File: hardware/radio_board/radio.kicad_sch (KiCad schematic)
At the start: 29 parts, among them J2 RF, J3 Shield, U1 MAX2769B

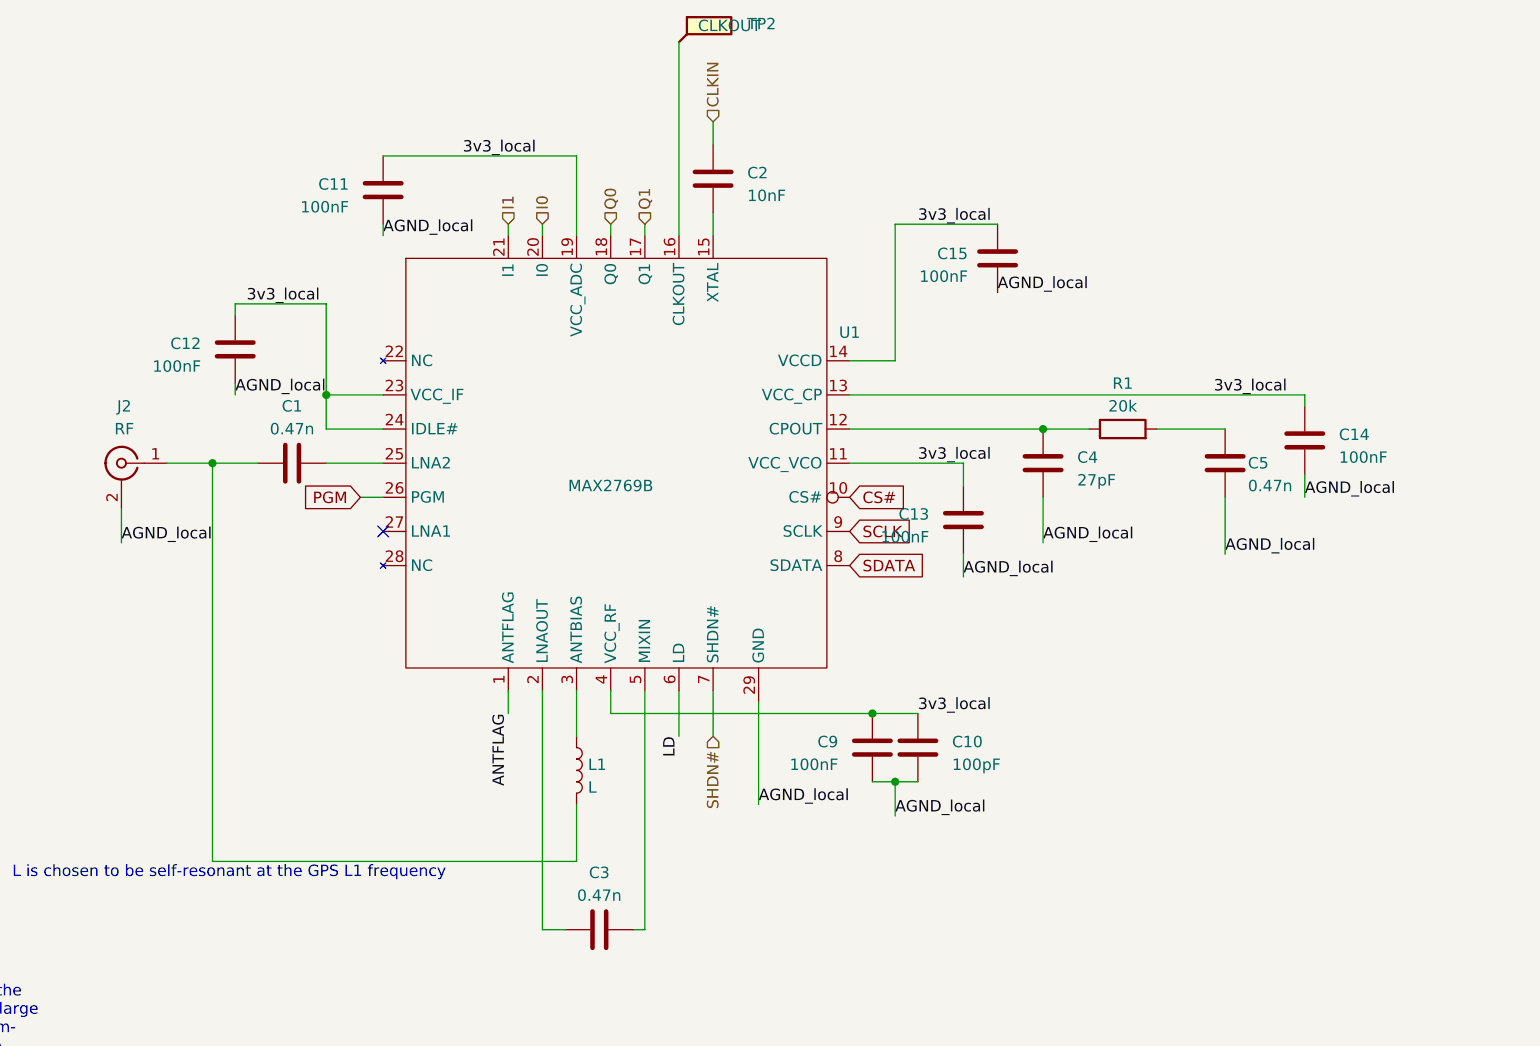
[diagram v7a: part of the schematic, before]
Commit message: Added a driver to the receive side of the clock
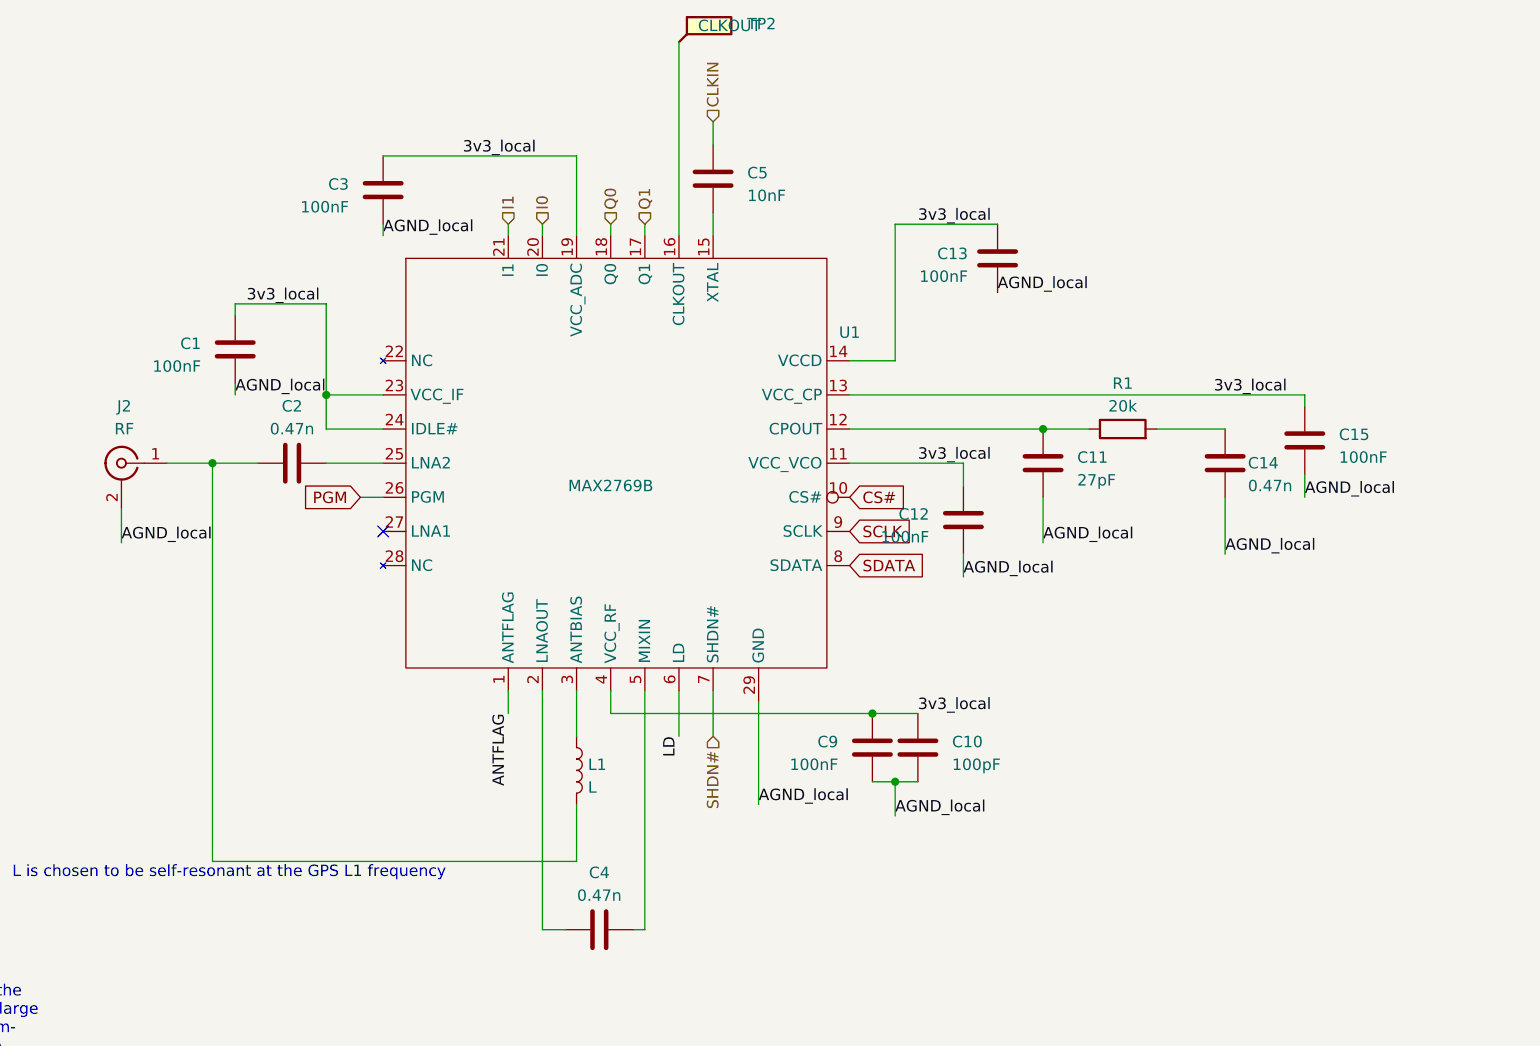
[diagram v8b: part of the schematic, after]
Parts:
- renumbered C12 to C1, C4 to C11, C13 to C12, C15 to C13, C5 to C14, C14 to C15, C1 to C2, C11 to C3, C3 to C4, C2 to C5
